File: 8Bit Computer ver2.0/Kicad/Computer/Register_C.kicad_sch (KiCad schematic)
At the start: 12 parts, among them IC134 SN74ABT245BDWR, IC135 SN74LVC1G32DBVR, IC136 SN74LVC1G14DBVR, IC137 SN74LVC1G14DBVR, IC138 SN74AHC74DR, IC139 SN74F283D, IC140 SN74F283D, IC141 SN74F283D, IC142 SN74LVC1G86DBVR, IC143 SN74ABT574ADWR, IC144 SN74ABT574ADWR, IC145 SN74LVC1G14DBVR

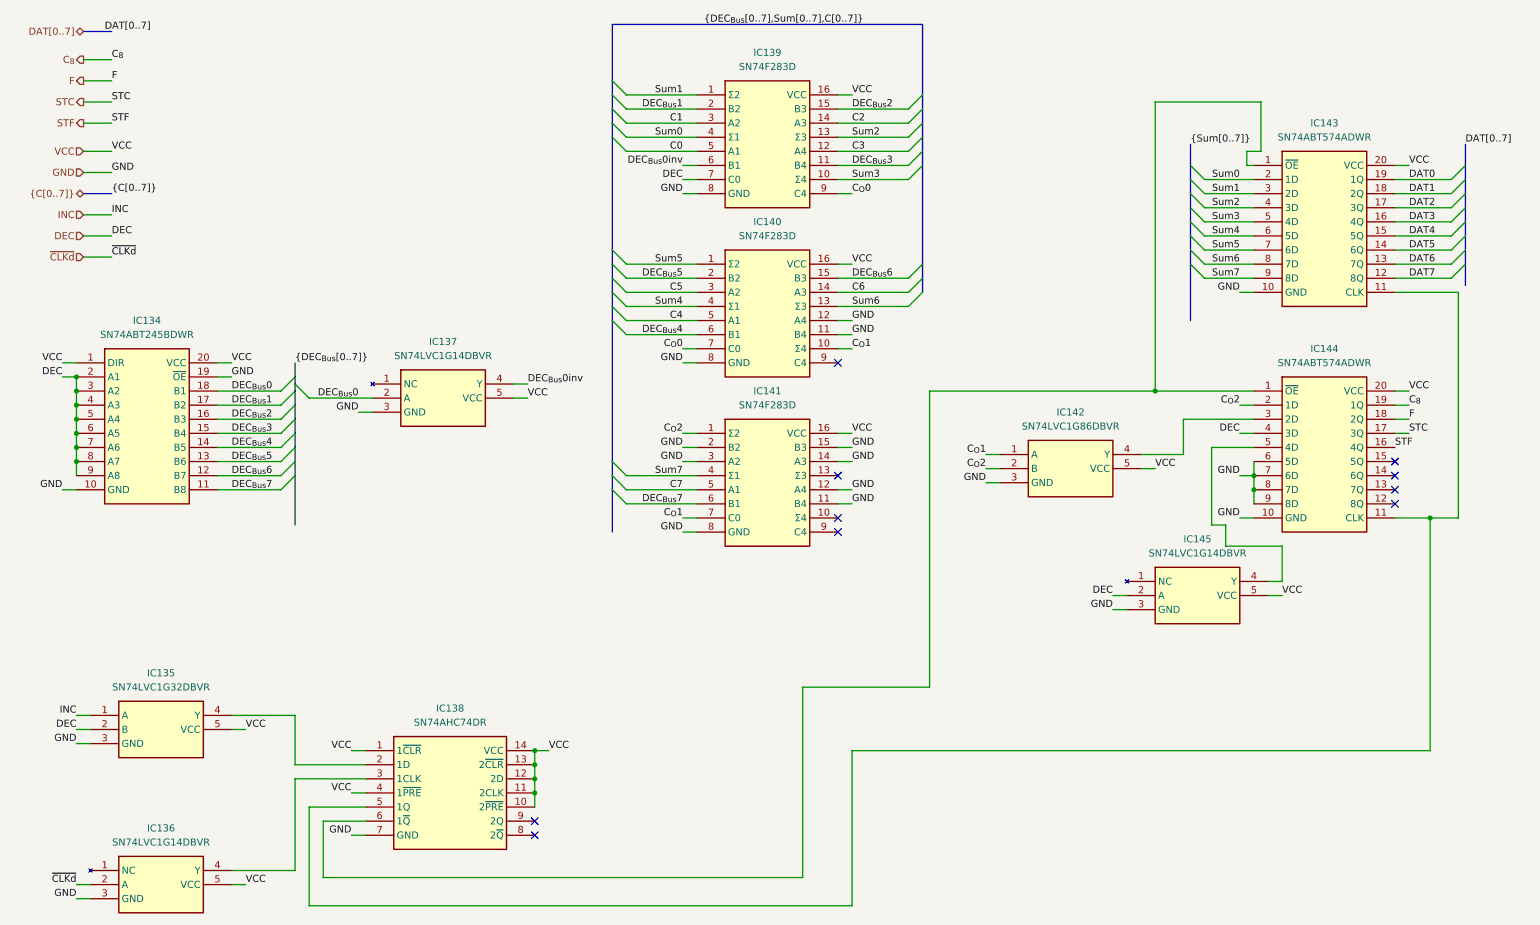
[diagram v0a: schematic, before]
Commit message: part 1 of changing to A4
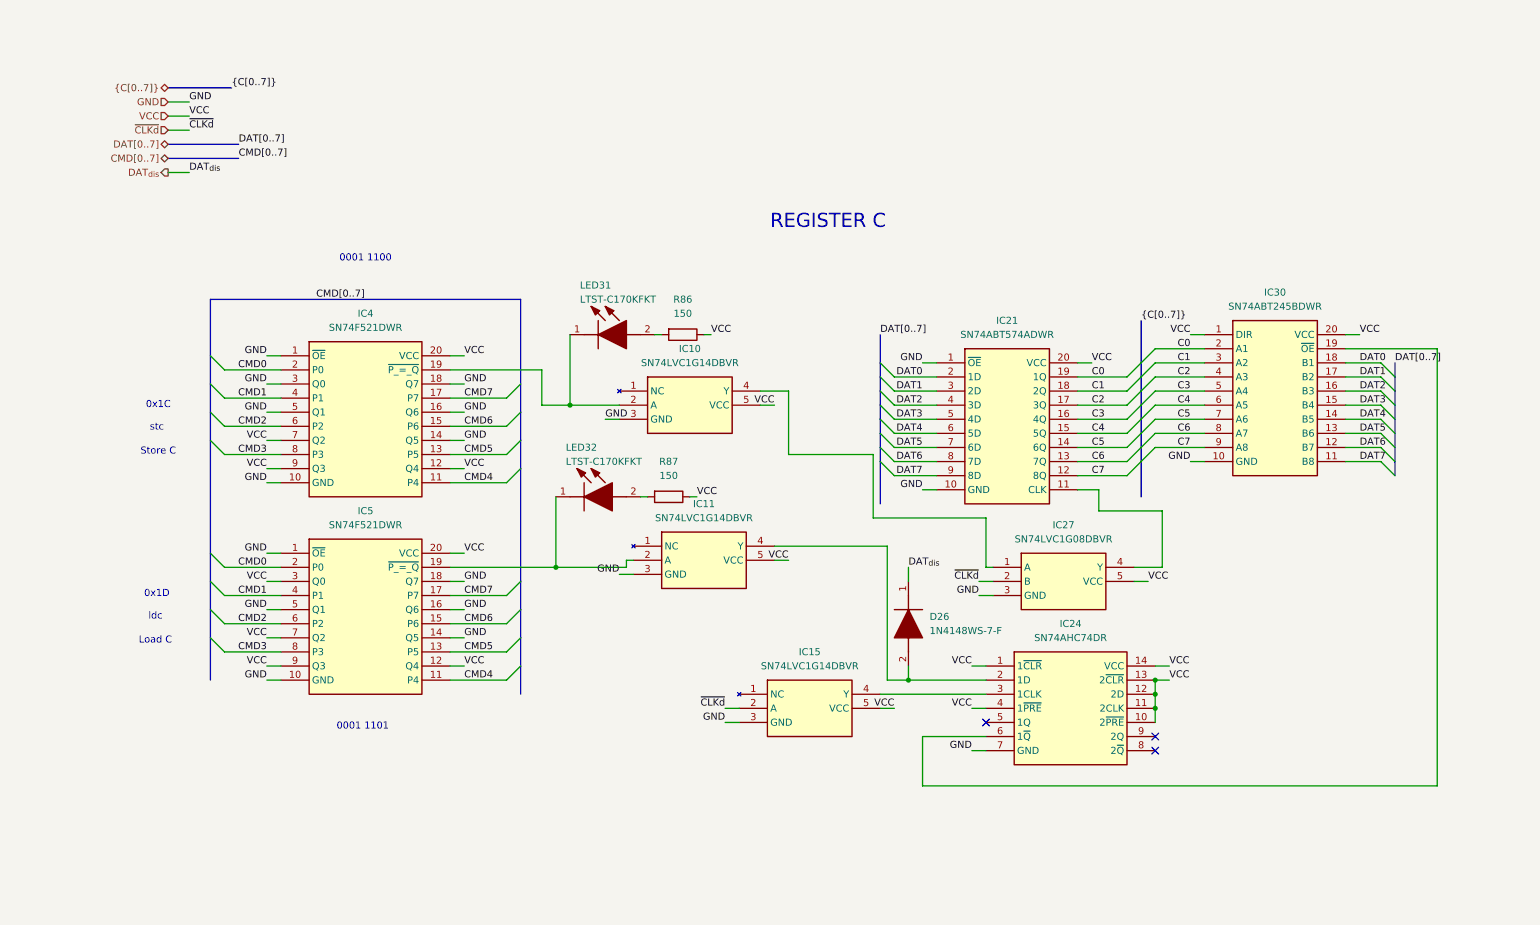
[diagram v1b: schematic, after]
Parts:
- removed IC134: SN74ABT245BDWR, Samacsys:SOIC127P1030X265-20N, symbol Samacsys:SN74ABT245BDWR
- removed IC135: SN74LVC1G32DBVR, Samacsys:SOT95P280X145-5N, symbol Samacsys:SN74LVC1G32DBVR
- removed IC136, IC137, IC145: SN74LVC1G14DBVR, Samacsys:SOT95P280X145-5N, symbol Samacsys:SN74LVC1G14DBVR
- removed IC138: SN74AHC74DR, Samacsys:SOIC127P600X175-14N, symbol Samacsys:SN74AHC74DR
- removed IC139, IC140, IC141: SN74F283D, Samacsys:SOIC127P600X175-16N, symbol Samacsys:SN74F283D
- removed IC142: SN74LVC1G86DBVR, Samacsys:SOT95P280X145-5N, symbol Samacsys:SN74LVC1G86DBVR
- removed IC143, IC144: SN74ABT574ADWR, Samacsys:SOIC127P1030X265-20N, symbol Samacsys:SN74ABT574ADWR
- added D26: 1N4148WS-7-F, Samacsys:SOD2513X120N, symbol Samacsys:1N4148WS-7-F
- added IC10, IC11, IC15: SN74LVC1G14DBVR, Samacsys:SOT95P280X145-5N, symbol Samacsys:SN74LVC1G14DBVR
- added IC21: SN74ABT574ADWR, Samacsys:SOIC127P1030X265-20N, symbol Samacsys:SN74ABT574ADWR
- added IC24: SN74AHC74DR, Samacsys:SOIC127P600X175-14N, symbol Samacsys:SN74AHC74DR
- added IC27: SN74LVC1G08DBVR, Samacsys:SOT95P280X145-5N, symbol Samacsys:SN74LVC1G08DBVR
- added IC30: SN74ABT245BDWR, Samacsys:SOIC127P1030X265-20N, symbol Samacsys:SN74ABT245BDWR
- added IC4, IC5: SN74F521DWR, Samacsys:SOIC127P1030X265-20N, symbol Samacsys:SN74F521DWR
- added LED31, LED32: LTST-C170KFKT, Samacsys:LEDC2012X120N, symbol Samacsys:LTST-C170KFKT
- added R86, R87: 150, Resistor_SMD:R_1206_3216Metric_Pad1.30x1.75mm_HandSolder, symbol Device:R
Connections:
- net C0: now also IC21.19 (1Q), IC30.2 (A1)
- net C1: now also IC21.18 (2Q), IC30.3 (A2)
- net C2: now also IC21.17 (3Q), IC30.4 (A3)
- net C3: now also IC21.16 (4Q), IC30.5 (A4)
- net C4: now also IC21.15 (5Q), IC30.6 (A5)
- net C5: now also IC21.14 (6Q), IC30.7 (A6)
- net C6: now also IC21.13 (7Q), IC30.8 (A7)
- net C7: now also IC21.12 (8Q), IC30.9 (A8)
- net DAT0: now also IC21.2 (1D), IC30.18 (B1)
- net DAT1: now also IC21.3 (2D), IC30.17 (B2)
- net DAT2: now also IC21.4 (3D), IC30.16 (B3)
- net DAT3: now also IC21.5 (4D), IC30.15 (B4)
- net DAT4: now also IC21.6 (5D), IC30.14 (B5)
- net DAT5: now also IC21.7 (6D), IC30.13 (B6)
- net DAT6: now also IC21.8 (7D), IC30.12 (B7)
- net DAT7: now also IC21.9 (8D), IC30.11 (B8)
- net GND: now also IC10.3 (GND), IC11.3 (GND), IC15.3 (GND), IC21.1 (~{OE}), IC21.10 (GND), IC24.7 (GND), IC27.3 (GND), IC30.10 (GND), IC4.1 (~{OE}), IC4.10 (GND), IC4.14 (Q5), IC4.16 (Q6), IC4.18 (Q7), IC4.3 (Q0), IC4.5 (Q1), IC5.1 (~{OE}), IC5.10 (GND), IC5.14 (Q5), IC5.16 (Q6), IC5.18 (Q7), IC5.5 (Q1)
- net VCC: now also IC10.5 (VCC), IC11.5 (VCC), IC15.5 (VCC), IC21.20 (VCC), IC24.1 (1~{CLR}), IC24.10 (2~{PRE}), IC24.11 (2CLK), IC24.12 (2D), IC24.13 (2~{CLR}), IC24.14 (VCC), IC24.4 (1~{PRE}), IC27.5 (VCC), IC30.1 (DIR), IC30.20 (VCC), IC4.12 (Q4), IC4.20 (VCC), IC4.7 (Q2), IC4.9 (Q3), IC5.12 (Q4), IC5.20 (VCC), IC5.3 (Q0), IC5.7 (Q2), IC5.9 (Q3), R86.1, R87.1
- net ~{CLKd}: now also IC15.2 (A), IC27.2 (B)
- new net: IC11.2 (A), IC5.19 (~{P_=_Q}), LED32.1 (K)
- new net: LED32.2 (A), R87.2
- new net: D26.2 (A), IC11.4 (Y), IC24.2 (1D)
- new net: IC15.4 (Y), IC24.3 (1CLK)
- new net: IC24.6 (1~{Q}), IC30.19 (~{OE})
- new net: IC21.11 (CLK), IC27.4 (Y)
- new net: LED31.2 (A), R86.2
- new net: IC10.4 (Y), IC27.1 (A)
- new net: IC10.2 (A), IC4.19 (~{P_=_Q}), LED31.1 (K)
- new net CMD0: IC4.2 (P0), IC5.2 (P0)
- new net CMD1: IC4.4 (P1), IC5.4 (P1)
- new net CMD2: IC4.6 (P2), IC5.6 (P2)
- new net CMD3: IC4.8 (P3), IC5.8 (P3)
- new net CMD4: IC4.11 (P4), IC5.11 (P4)
- new net CMD5: IC4.13 (P5), IC5.13 (P5)
- new net CMD6: IC4.15 (P6), IC5.15 (P6)
- new net CMD7: IC4.17 (P7), IC5.17 (P7)
- new net DAT_{dis}: D26.1 (K)
- no-connect marks 10 -> 3
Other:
- note added: "0001 1100"
- note added: "0001 1101"
- note added: "0x1C"
- note added: "0x1D"
- note added: "Load C"
- note added: "REGISTER C"
- note added: "Store C"
- note added: "ldc"
- note added: "stc"

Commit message: changed page numbers, every schematic is now A4
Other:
- title: (none) -> ${SHEETNAME}
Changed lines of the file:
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@@
 	(generator_version "9.0")
 	(paper "A4")
+	(title_block
+		(title "${SHEETNAME}")
+		(date "2026-03-21")
+		(rev "2.7")
+	)
 	(text "0x1D\n\n"
 		(exclude_from_sim no)
